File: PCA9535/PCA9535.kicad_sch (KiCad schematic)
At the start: 16 parts, among them J1 Conn_01x04, J2 Conn_01x04, J3 Conn_02x05_Odd_Even, J4 Conn_01x01, J6 Conn_02x05_Odd_Even, U1 PCA9535DBR

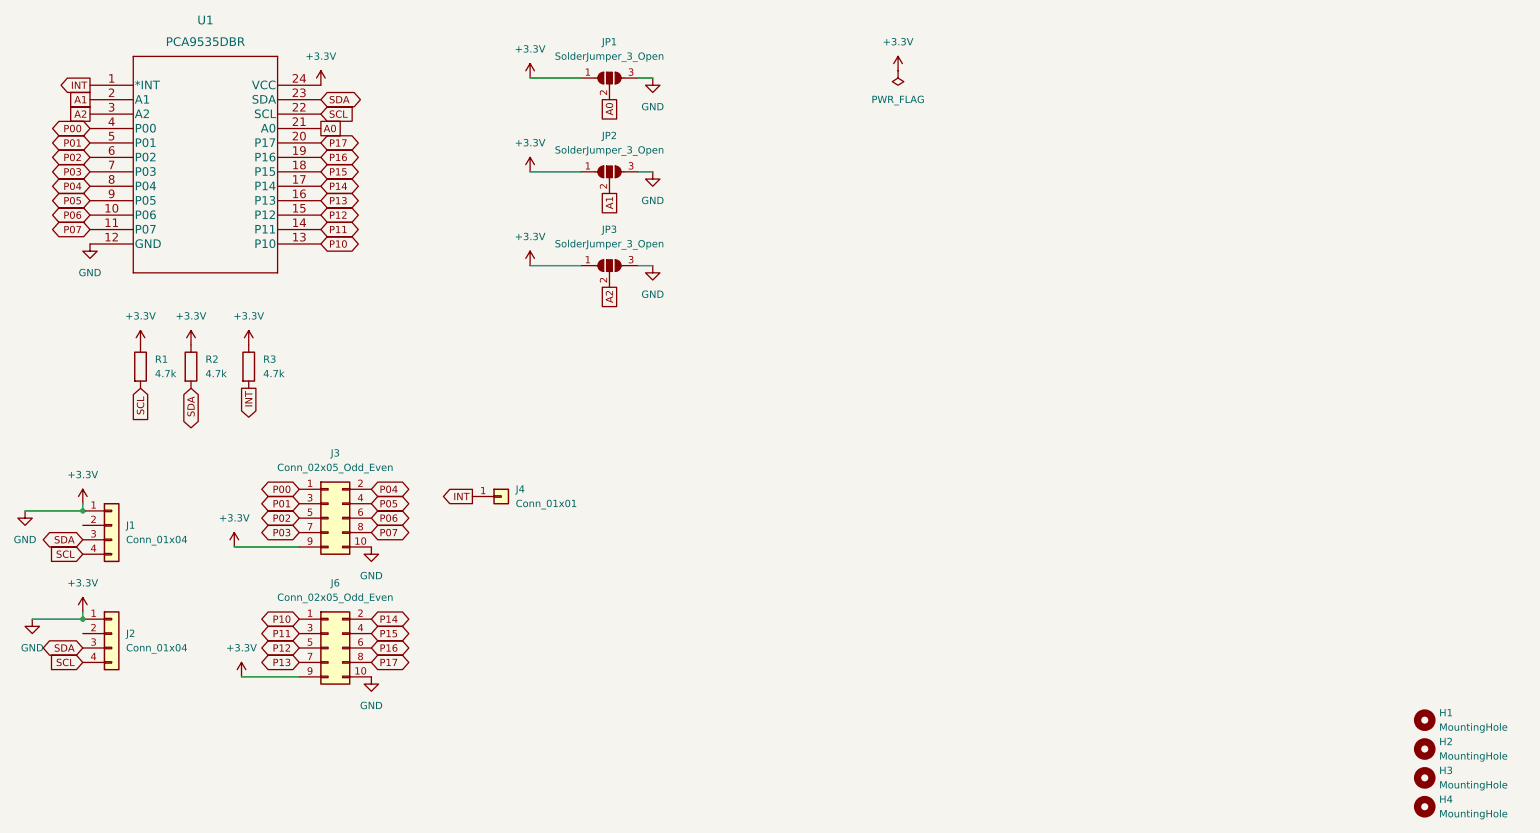
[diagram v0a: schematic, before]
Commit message: Finalizing the 16pin expander
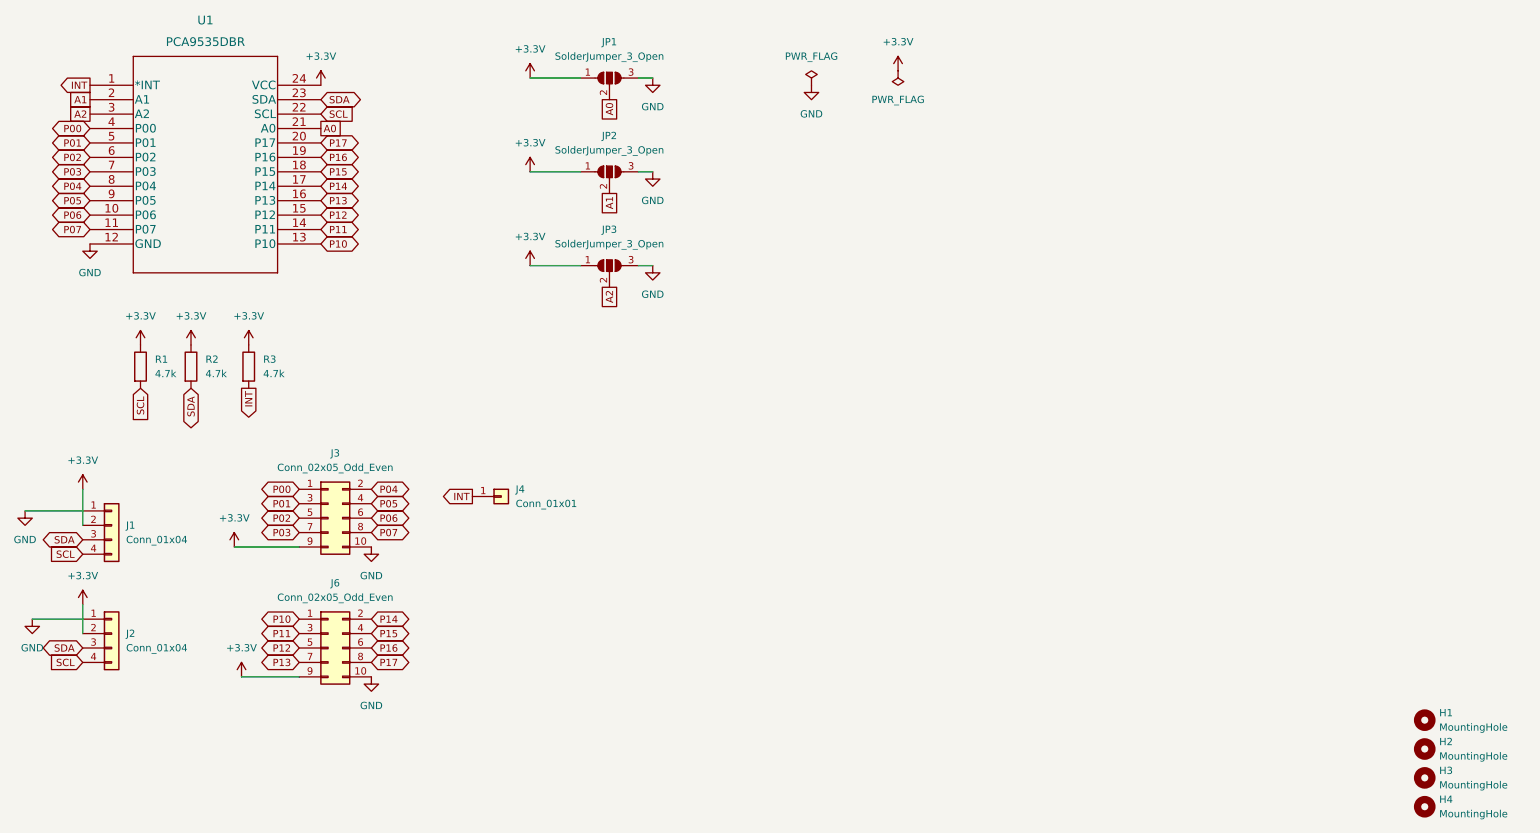
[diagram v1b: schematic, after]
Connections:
- net +3.3V: now also J1.2 (Pin_2), J2.2 (Pin_2); no longer J1.1 (Pin_1), J2.1 (Pin_1), J3.10 (Pin_10), J6.10 (Pin_10), JP1.3 (B), JP2.3 (B), JP3.3 (B), U1.12 (GND)
- new net GND: J1.1 (Pin_1), J2.1 (Pin_1), J3.10 (Pin_10), J6.10 (Pin_10), JP1.3 (B), JP2.3 (B), JP3.3 (B), U1.12 (GND)
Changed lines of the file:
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@@
     (company "Because I'm Clever")
   )
-  (junction (at 29.21 128.27) (diameter 0) (color 0 0 0 0)
-  )
-  (junction (at 29.21 109.22) (diameter 0) (color 0 0 0 0)
-  )
   (wire (pts (xy 107.95 33.02) (xy 116.84 33.02))
     (stroke (width 0) (type default) (color 0 0 0 0))
@@
     (stroke (width 0) (type default) (color 0 0 0 0))
   )
-  (wire (pts (xy 29.21 127) (xy 29.21 128.27))
+  (wire (pts (xy 29.21 105.41) (xy 29.21 111.76))
+    (stroke (width 0) (type default) (color 0 0 0 0))
+  )
+  (wire (pts (xy 29.21 125.73) (xy 29.21 130.81))
     (stroke (width 0) (type default) (color 0 0 0 0))
   )
@@
   )
   (wire (pts (xy 55.88 115.57) (xy 67.31 115.57))
-    (stroke (width 0) (type default) (color 0 0 0 0))
-  )
-  (wire (pts (xy 29.21 107.95) (xy 29.21 109.22))
     (stroke (width 0) (type default) (color 0 0 0 0))
   )
@@
     (pin "4")
   )
+  (symbol (lib_id "power:GND") (at 157.48 34.29 0) (unit 1)
+    (in_bom yes) (on_board yes) (fields_autoplaced)
+    (property "Reference" "#PWR0105" (id 0) (at 157.48 40.64 0)
+      (effects (font (size 1.27 1.27)) hide)
+    )
+    (property "Value" "GND" (id 1) (at 157.48 39.37 0))
+    (property "Footprint" "" (id 2) (at 157.48 34.29 0)
+      (effects (font (size 1.27 1.27)) hide)
+    )
+    (property "Datasheet" "" (id 3) (at 157.48 34.29 0)
+      (effects (font (size 1.27 1.27)) hide)
+    )
+    (pin "1")
+  )
   (symbol (lib_id "Jumper:SolderJumper_3_Open") (at 121.92 66.04 0) (unit 1)
     (in_bom yes) (on_board yes) (fields_autoplaced)
@@
     (pin "3")
   )
-  (symbol (lib_id "power:+3.3V") (at 29.21 107.95 0) (unit 1)
-    (in_bom yes) (on_board yes) (fields_autoplaced)
-    (property "Reference" "#PWR0101" (id 0) (at 29.21 111.76 0)
-      (effects (font (size 1.27 1.27)) hide)
-    )
-    (property "Value" "+3.3V" (id 1) (at 29.21 102.87 0))
-    (property "Footprint" "" (id 2) (at 29.21 107.95 0)
-      (effects (font (size 1.27 1.27)) hide)
-    )
-    (property "Datasheet" "" (id 3) (at 29.21 107.95 0)
+  (symbol (lib_id "power:+3.3V") (at 29.21 105.41 0) (unit 1)
+    (in_bom yes) (on_board yes) (fields_autoplaced)
+    (property "Reference" "#PWR0101" (id 0) (at 29.21 109.22 0)
+      (effects (font (size 1.27 1.27)) hide)
+    )
+    (property "Value" "+3.3V" (id 1) (at 29.21 100.33 0))
+    (property "Footprint" "" (id 2) (at 29.21 105.41 0)
+      (effects (font (size 1.27 1.27)) hide)
+    )
+    (property "Datasheet" "" (id 3) (at 29.21 105.41 0)
       (effects (font (size 1.27 1.27)) hide)
     )
@@
     (pin "9")
   )
+  (symbol (lib_id "power:PWR_FLAG") (at 157.48 34.29 0) (unit 1)
+    (in_bom yes) (on_board yes) (fields_autoplaced)
+    (property "Reference" "#FLG0101" (id 0) (at 157.48 32.385 0)
+      (effects (font (size 1.27 1.27)) hide)
+    )
+    (property "Value" "PWR_FLAG" (id 1) (at 157.48 29.21 0))
+    (property "Footprint" "" (id 2) (at 157.48 34.29 0)
+      (effects (font (size 1.27 1.27)) hide)
+    )
+    (property "Datasheet" "~" (id 3) (at 157.48 34.29 0)
+      (effects (font (size 1.27 1.27)) hide)
+    )
+    (pin "1")
+  )
   (symbol (lib_id "power:+3.3V") (at 55.88 115.57 0) (unit 1)
     (in_bom yes) (on_board yes)
@@
     (pin "1")
   )
-  (symbol (lib_id "power:+3.3V") (at 29.21 127 0) (unit 1)
-    (in_bom yes) (on_board yes) (fields_autoplaced)
-    (property "Reference" "#PWR0104" (id 0) (at 29.21 130.81 0)
-      (effects (font (size 1.27 1.27)) hide)
-    )
-    (property "Value" "+3.3V" (id 1) (at 29.21 121.92 0))
-    (property "Footprint" "" (id 2) (at 29.21 127 0)
-      (effects (font (size 1.27 1.27)) hide)
-    )
-    (property "Datasheet" "" (id 3) (at 29.21 127 0)
+  (symbol (lib_id "power:+3.3V") (at 29.21 125.73 0) (unit 1)
+    (in_bom yes) (on_board yes) (fields_autoplaced)
+    (property "Reference" "#PWR0104" (id 0) (at 29.21 129.54 0)
+      (effects (font (size 1.27 1.27)) hide)
+    )
+    (property "Value" "+3.3V" (id 1) (at 29.21 120.65 0))
+    (property "Footprint" "" (id 2) (at 29.21 125.73 0)
+      (effects (font (size 1.27 1.27)) hide)
+    )
+    (property "Datasheet" "" (id 3) (at 29.21 125.73 0)
       (effects (font (size 1.27 1.27)) hide)
     )
@@
       (reference "#FLG01") (unit 1) (value "PWR_FLAG") (footprint "")
     )
+    (path "/9edb0ba0-64f4-4ab4-a3f4-329bd74d7974"
+      (reference "#FLG0101") (unit 1) (value "PWR_FLAG") (footprint "")
+    )
     (path "/825c4cfa-91a4-4ac6-939f-48b24927f896"
       (reference "#PWR01") (unit 1) (value "+3.3V") (footprint "")
@@
       (reference "#PWR0104") (unit 1) (value "+3.3V") (footprint "")
     )
+    (path "/181d5a35-5284-46cb-8b3d-03bb70b78cae"
+      (reference "#PWR0105") (unit 1) (value "GND") (footprint "")
+    )
     (path "/92e246e9-00cd-457a-8661-d7c41ec0c8f0"

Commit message: syncing
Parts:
- J1, J2: footprint Connector_JST:JST_SH_BM04B-SRSS-TB_1x04-1MP_P1.00mm_Vertical -> Connector_JST:JST_SH_SM04B-SRSS-TB_1x04-1MP_P1.00mm_Horizontal
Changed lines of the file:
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@@
       (effects (font (size 1.27 1.27)) (justify left))
     )
-    (property "Footprint" "Connector_JST:JST_SH_BM04B-SRSS-TB_1x04-1MP_P1.00mm_Vertical" (id 2) (at 34.29 130.81 0)
+    (property "Footprint" "Connector_JST:JST_SH_SM04B-SRSS-TB_1x04-1MP_P1.00mm_Horizontal" (id 2) (at 34.29 130.81 0)
       (effects (font (size 1.27 1.27)) hide)
     )
@@
       (effects (font (size 1.27 1.27)) (justify left))
     )
-    (property "Footprint" "Connector_JST:JST_SH_BM04B-SRSS-TB_1x04-1MP_P1.00mm_Vertical" (id 2) (at 34.29 111.76 0)
+    (property "Footprint" "Connector_JST:JST_SH_SM04B-SRSS-TB_1x04-1MP_P1.00mm_Horizontal" (id 2) (at 34.29 111.76 0)
       (effects (font (size 1.27 1.27)) hide)
     )
@@
     )
     (path "/2d4d87f0-d617-4639-8967-fc4d84362ff9"
-      (reference "J1") (unit 1) (value "Conn_01x04") (footprint "Connector_JST:JST_SH_BM04B-SRSS-TB_1x04-1MP_P1.00mm_Vertical")
+      (reference "J1") (unit 1) (value "Conn_01x04") (footprint "Connector_JST:JST_SH_SM04B-SRSS-TB_1x04-1MP_P1.00mm_Horizontal")
     )
     (path "/0b3d3461-b7d3-4182-896a-ee33de331d45"
-      (reference "J2") (unit 1) (value "Conn_01x04") (footprint "Connector_JST:JST_SH_BM04B-SRSS-TB_1x04-1MP_P1.00mm_Vertical")
+      (reference "J2") (unit 1) (value "Conn_01x04") (footprint "Connector_JST:JST_SH_SM04B-SRSS-TB_1x04-1MP_P1.00mm_Horizontal")
     )
     (path "/a7c1bda0-6d30-46ff-b19d-e5df136776c9"
